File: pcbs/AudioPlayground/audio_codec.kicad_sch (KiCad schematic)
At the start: 19 parts, among them U4 MAX9867

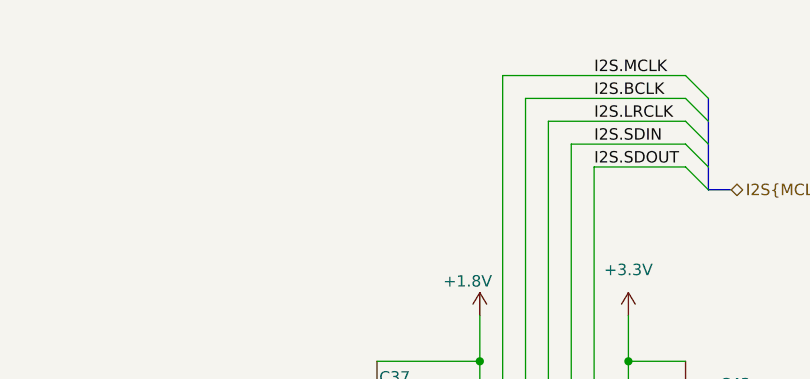
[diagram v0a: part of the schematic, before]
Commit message: updated footprints, added i2s testpoints
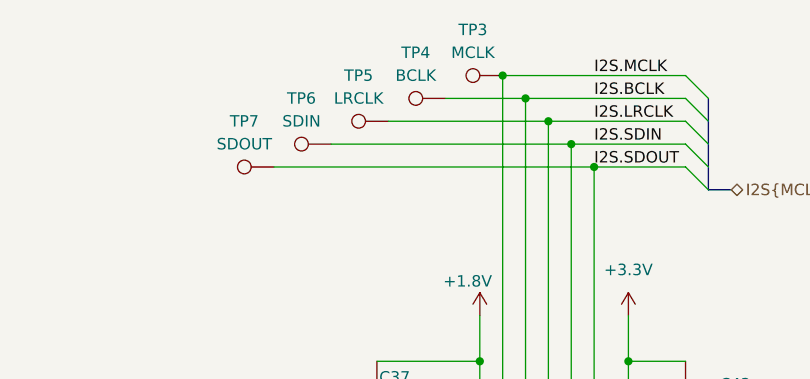
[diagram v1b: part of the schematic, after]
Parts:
- added TP3: MCLK, TestPoint:TestPoint_Pad_D1.0mm, symbol Connector:TestPoint
- added TP4: BCLK, TestPoint:TestPoint_Pad_D1.0mm, symbol Connector:TestPoint
- added TP5: LRCLK, TestPoint:TestPoint_Pad_D1.0mm, symbol Connector:TestPoint
- added TP6: SDIN, TestPoint:TestPoint_Pad_D1.0mm, symbol Connector:TestPoint
- added TP7: SDOUT, TestPoint:TestPoint_Pad_D1.0mm, symbol Connector:TestPoint
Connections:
- net I2S.BCLK: now also TP4.1
- net I2S.LRCLK: now also TP5.1
- net I2S.MCLK: now also TP3.1
- net I2S.SDIN: now also TP6.1
- net I2S.SDOUT: now also TP7.1

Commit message: Add LCSC and fix RF
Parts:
- C31, C33, C34, C37, C38, C39, C42: LCSC (none) -> C52923
- C32: LCSC (none) -> C12530
- C40, C41: value 0.47uF -> 470nF; LCSC (none) -> C47339
- C54, C57: value 0.22UF -> 220nF; LCSC (none) -> C16772
- C55, C56: LCSC (none) -> C412252
- R10, R9: LCSC (none) -> C25900
- R11: LCSC (none) -> C25744
- R7: LCSC (none) -> C25879
- TP3, TP4, TP5, TP6, TP7: now left out of the parts list
- U4: LCSC (none) -> C2649368
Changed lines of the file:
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@@
 			)
 		)
-		(property "Value" "0.47uF"
+		(property "Value" "470nF"
 			(at 210.566 130.556 0)
 			(effects
@@
 			)
 		)
+		(property "LCSC" "C47339"
+			(at 217.17 128.27 0)
+			(effects
+				(font
+					(size 1.27 1.27)
+				)
+				(hide yes)
+			)
+		)
 		(pin "2"
 		)
@@
 		(unit 1)
 		(exclude_from_sim no)
-		(in_bom yes)
+		(in_bom no)
 		(on_board yes)
 		(dnp no)
@@
 			)
 		)
-		(property "Value" "0.22UF"
+		(property "Value" "220nF"
 			(at 157.48 139.6999 0)
 			(effects
@@
 			)
 		)
+		(property "LCSC" "C16772"
+			(at 153.67 138.43 0)
+			(effects
+				(font
+					(size 1.27 1.27)
+				)
+				(hide yes)
+			)
+		)
 		(pin "2"
 		)
@@
 			)
 		)
+		(property "LCSC" "C52923"
+			(at 97.79 99.06 0)
+			(effects
+				(font
+					(size 1.27 1.27)
+				)
+				(hide yes)
+			)
+		)
 		(pin "2"
 		)
@@
 		(unit 1)
 		(exclude_from_sim no)
-		(in_bom yes)
+		(in_bom no)
 		(on_board yes)
 		(dnp no)
@@
 			)
 		)
+		(property "LCSC" "C52923"
+			(at 121.92 106.68 0)
+			(effects
+				(font
+					(size 1.27 1.27)
+				)
+				(hide yes)
+			)
+		)
 		(pin "2"
 		)
@@
 			)
 		)
+		(property "LCSC" "C25879"
+			(at 147.32 156.21 90)
+			(effects
+				(font
+					(size 1.27 1.27)
+				)
+				(hide yes)
+			)
+		)
 		(pin "1"
 		)
@@
 			)
 		)
-		(property "Value" "0.22UF"
+		(property "Value" "220nF"
 			(at 154.94 152.3999 0)
 			(effects
@@
 			)
 		)
+		(property "LCSC" "C16772"
+			(at 151.13 151.13 0)
+			(effects
+				(font
+					(size 1.27 1.27)
+				)
+				(hide yes)
+			)
+		)
 		(pin "2"
 		)
@@
 			)
 		)
+		(property "LCSC" "C52923"
+			(at 134.62 62.23 0)
+			(effects
+				(font
+					(size 1.27 1.27)
+				)
+				(hide yes)
+			)
+		)
 		(pin "1"
 		)
@@
 			)
 		)
+		(property "LCSC" "C25744"
+			(at 118.11 92.71 90)
+			(effects
+				(font
+					(size 1.27 1.27)
+				)
+				(hide yes)
+			)
+		)
 		(pin "1"
 		)
@@
 			)
 		)
+		(property "LCSC" "C412252"
+			(at 184.15 90.17 90)
+			(effects
+				(font
+					(size 1.27 1.27)
+				)
+				(hide yes)
+			)
+		)
 		(pin "1"
 		)
@@
 			)
 		)
+		(property "LCSC" "C52923"
+			(at 143.51 172.72 0)
+			(effects
+				(font
+					(size 1.27 1.27)
+				)
+				(hide yes)
+			)
+		)
 		(pin "2"
 		)
@@
 			)
 		)
+		(property "LCSC" "C52923"
+			(at 114.3 104.14 0)
+			(effects
+				(font
+					(size 1.27 1.27)
+				)
+				(hide yes)
+			)
+		)
 		(pin "2"
 		)
@@
 		(unit 1)
 		(exclude_from_sim no)
-		(in_bom yes)
+		(in_bom no)
 		(on_board yes)
 		(dnp no)
@@
 			)
 		)
+		(property "LCSC" "C52923"
+			(at 168.91 62.23 0)
+			(effects
+				(font
+					(size 1.27 1.27)
+				)
+				(hide yes)
+			)
+		)
 		(pin "2"
 		)
@@
 			)
 		)
+		(property "LCSC" "C52923"
+			(at 213.36 92.71 0)
+			(effects
+				(font
+					(size 1.27 1.27)
+				)
+				(hide yes)
+			)
+		)
 		(pin "2"
 		)
@@
 		(unit 1)
 		(exclude_from_sim no)
-		(in_bom yes)
+		(in_bom no)
 		(on_board yes)
 		(dnp no)
@@
 			)
 		)
+		(property "LCSC" "C25900"
+			(at 113.03 72.39 0)
+			(effects
+				(font
+					(size 1.27 1.27)
+				)
+				(hide yes)
+			)
+		)
 		(pin "2"
 		)
@@
 			)
 		)
-		(property "Value" "0.47uF"
+		(property "Value" "470nF"
 			(at 224.028 131.064 0)
 			(effects
@@
 			)
 		)
+		(property "LCSC" "C47339"
+			(at 223.52 128.27 0)
+			(effects
+				(font
+					(size 1.27 1.27)
+				)
+				(hide yes)
+			)
+		)
 		(pin "2"
 		)
@@
 			)
 		)
+		(property "LCSC" "C412252"
+			(at 184.15 97.79 90)
+			(effects
+				(font
+					(size 1.27 1.27)
+				)
+				(hide yes)
+			)
+		)
 		(pin "1"
 		)
@@
 			)
 		)
+		(property "LCSC" "C25900"
+			(at 104.14 72.39 0)
+			(effects
+				(font
+					(size 1.27 1.27)
+				)
+				(hide yes)
+			)
+		)
 		(pin "2"
 		)
@@
 			)
 		)
+		(property "LCSC" "C12530"
+			(at 105.41 101.6 0)
+			(effects
+				(font
+					(size 1.27 1.27)
+				)
+				(hide yes)
+			)
+		)
 		(pin "2"
 		)
@@
 		(unit 1)
 		(exclude_from_sim no)
-		(in_bom yes)
+		(in_bom no)
 		(on_board yes)
 		(dnp no)
@@
 			(at 147.32 99.06 0)
 			(effects
+				(font
+					(size 1.27 1.27)
+				)
+				(hide yes)
+			)
+		)
+		(property "LCSC" "C2649368"
+			(at 147.32 99.06 0)
+			(effects

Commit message: Fix Codec IRQ
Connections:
- net CODECIRQ: now reaches R11.2, U4.4 (IRQ)
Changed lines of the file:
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@@
+	(wire
+		(pts
+			(xy 92.71 91.44) (xy 87.63 91.44)
+		)
+		(stroke
+			(width 0)
+			(type default)
+		)
+	)
 	(wire
 		(pts
@@
 		)
 	)
+	(label "IRQ"
+		(at 123.19 92.71 0)
+		(effects
+			(font
+				(size 1.27 1.27)
+			)
+			(justify left bottom)
+		)
+	)
 	(label "I2S.SDIN"
 		(at 158.75 34.29 0)
@@
 			)
 			(justify left bottom)
+		)
+	)
+	(label "IRQ"
+		(at 92.71 91.44 180)
+		(effects
+			(font
+				(size 1.27 1.27)
+			)
+			(justify right bottom)
 		)
 	)
@@
 		)
 	)
+	(hierarchical_label "CODECIRQ"
+		(shape output)
+		(at 87.63 91.44 180)
+		(effects
+			(font
+				(size 1.27 1.27)
+			)
+			(justify right)
+		)
+	)

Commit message: Improve Optic
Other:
- title: (none) -> LE Audio Playground
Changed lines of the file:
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@@
 	(generator_version "9.0")
 	(paper "A4")
+	(title_block
+		(title "LE Audio Playground")
+		(rev "2.2")
+	)
 	(junction
 		(at 148.59 26.67)
